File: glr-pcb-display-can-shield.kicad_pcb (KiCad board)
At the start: 2 copper layers, 46 x 90 mm, 11 parts, among them CN12 Conn_02x08_Odd_Even, CN6 Conn_01x08, CN8 Conn_01x06, IC1 L9615D013TR, IC2 LF80CDT-TR, J1 Screw_Terminal_01x04, J2 Screw_Terminal_01x08

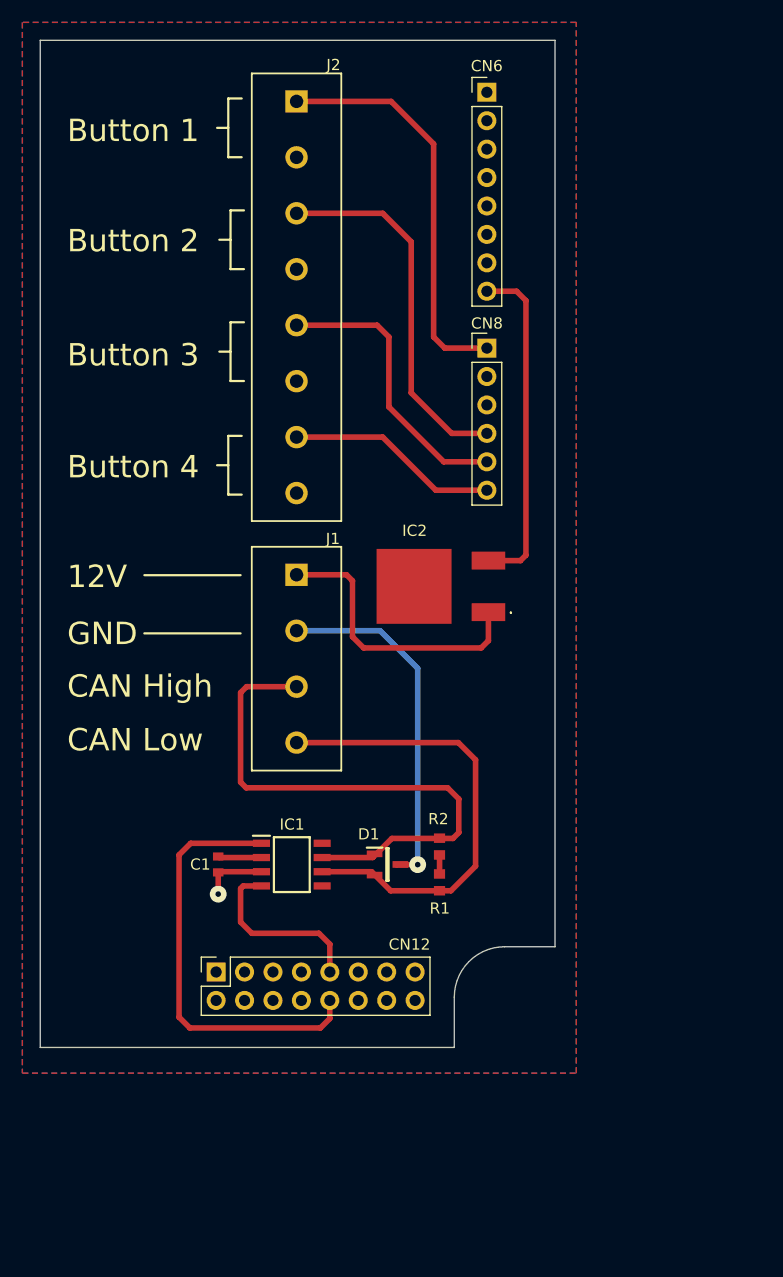
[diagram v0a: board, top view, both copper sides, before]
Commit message: update can shield for new car
* provide more inputs for buttons and rotary encoders (not sure about that, big connector needed now)
* apply new can setup
* add new voltage transformer
* add full arduino headers
* m12a 4pin for power and can
* make board full size
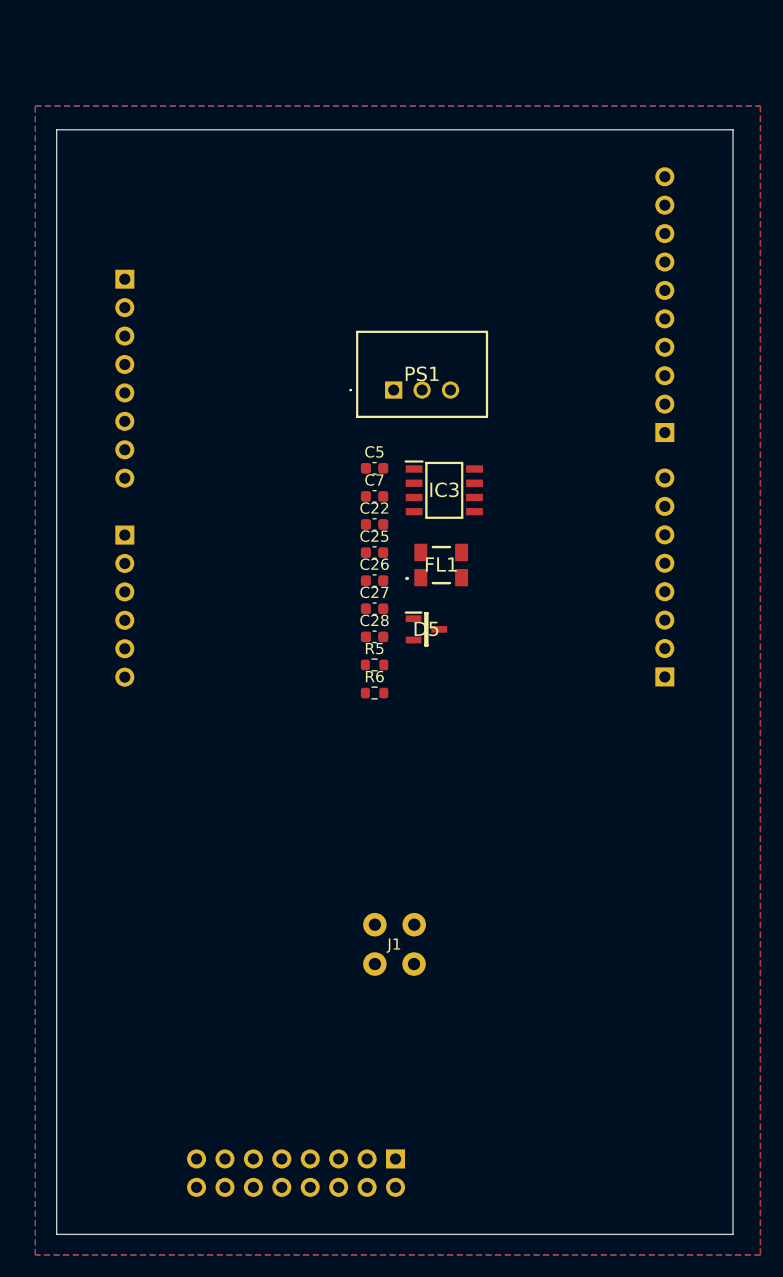
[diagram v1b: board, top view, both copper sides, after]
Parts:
- removed C1: 0.1μF 50V, SamacSys_Parts:CAPC1608X90N
- removed D1: ESDCAN01-2BLY, SamacSys_Parts:SOT95P255X125-3N
- removed IC1: L9615D013TR, SamacSys_Parts:SOIC127P600X175-8N
- removed IC2: LF80CDT-TR, SamacSys_Parts:LF80CDTTR
- removed J2: Screw_Terminal_01x08, GLR_KiCad_Library:WECO-950-FB-08
- removed R1, R2: 68.0 Ω, SamacSys_Parts:RESC1608X50N
- added C22: 100n, Capacitor_SMD:C_0603_1608Metric, F.Cu at (147.5, 88.5)
- added C25: 100p, Capacitor_SMD:C_0603_1608Metric, F.Cu at (147.5, 91.0)
- added C26: 100p, Capacitor_SMD:C_0603_1608Metric, F.Cu at (147.5, 93.5)
- added C27: 100p, Capacitor_SMD:C_0603_1608Metric, F.Cu at (147.5, 96.0)
- added C28: 100p, Capacitor_SMD:C_0603_1608Metric, F.Cu at (147.5, 98.5)
- added C5: 100n, Capacitor_SMD:C_0603_1608Metric, F.Cu at (147.5, 83.5)
- added C7: 100n, Capacitor_SMD:C_0603_1608Metric, F.Cu at (147.5, 86.0)
- added CN5: Conn_01x10, Connector_PinHeader_2.54mm:PinHeader_1x10_P2.54mm_Vertical, B.Cu at (173.4, 80.3)
- added CN7: Conn_01x08, Connector_PinHeader_2.54mm:PinHeader_1x08_P2.54mm_Vertical, B.Cu at (173.4, 102.1)
- added D5: ESDCAN01-2BLY, SamacSys_Parts:SOT95P255X125-3N, F.Cu at (152.1, 97.8)
- added FL1: Choke, SamacSys_Parts:744235510, F.Cu at (153.4, 92.1)
- added IC3: ATA6561-GAQW-N, SamacSys_Parts:SOIC127P600X175-8N, F.Cu at (153.7, 85.4)
- added PS1: RBT05W24S6V5, SamacSys_Parts:RBT05W24S6V5, F.Cu at (149.2, 76.5)
- added R5: 60, Resistor_SMD:R_0603_1608Metric, F.Cu at (147.5, 101.0)
- added R6: 60, Resistor_SMD:R_0603_1608Metric, F.Cu at (147.5, 103.5)
- CN12, CN6, CN8: moved to B.Cu
- J1: value Screw_Terminal_01x04 -> Conn_02x02_Counter_Clockwise_Shielded; footprint GLR_KiCad_Library:WECO-950-FB-04 -> GLR_KiCad_Library:M12A-04P
- moved CN6 36.4 mm to (125.2, 66.6), turned to 180 degrees
- moved CN8 36.4 mm to (125.2, 89.4), turned to 180 degrees
- moved CN12 23.2 mm to (149.3, 145.2)
- moved J1 17.6 mm to (149.2, 126.0), turned to 0 degrees
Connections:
- CN12 pad 10: /Tx -> can_TX
- CN12 pad 3: unconnected-(CN12-Pin_3-Pad3) -> pot1
- CN12 pad 5: unconnected-(CN12-Pin_5-Pad5) -> pot2
- CN12 pad 6: unconnected-(CN12-Pin_6-Pad6) -> pot3
- CN12 pad 9: /Rx -> can_RX
- CN8 pad 1: /button1 -> button1
- CN8 pad 4: /button2 -> button2
- CN8 pad 5: /button3 -> button3
- CN8 pad 6: /button4 -> button4
- J1 pad 1: /+12V -> GND
- J1 pad 2: GND -> can_H
- J1 pad 3: /CAN H -> can_L
- J1 pad 4: /CAN L -> +24V
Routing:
- net /CAN H: track 49.5 -> 0.00 mm
- net /CAN L: track 41.5 -> 0.00 mm
- net /Tx: track 38.1 -> 0.00 mm
- net /button1: track 36.4 -> 0.00 mm
- net GND: track 35.6 -> 0.00 mm, vias 1 -> 0
- net /button2: track 33.1 -> 0.00 mm
- net +8V: track 30.1 -> 0.00 mm
- net /button3: track 25.9 -> 0.00 mm
- net /+12V: track 25.6 -> 0.00 mm
- net /button4: track 19.1 -> 0.00 mm
- net /Rx: track 16.2 -> 0.00 mm
- net +5V: track 5.83 -> 0.00 mm, vias 1 -> 0
- net Net-(R1-Pad2): track 1.61 -> 0.00 mm
- added copper zone on F.Cu, net +5V
- added copper zone on B.Cu, net GND
- removed copper zone on B.Cu, net +5V
- removed copper zone on F.Cu, net GND
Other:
- board size 46 x 90 mm -> 60.4 x 98.7 mm
- board text removed: "12V"
- board text removed: "Button 1"
- board text removed: "Button 2"
- board text removed: "Button 3"
- board text removed: "Button 4"
- board text removed: "CAN High"
- board text removed: "CAN Low"
- board text removed: "GND"

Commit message: use absolute rotary encoders
* use more pins add dsub connector
* add documents
* routing should be done
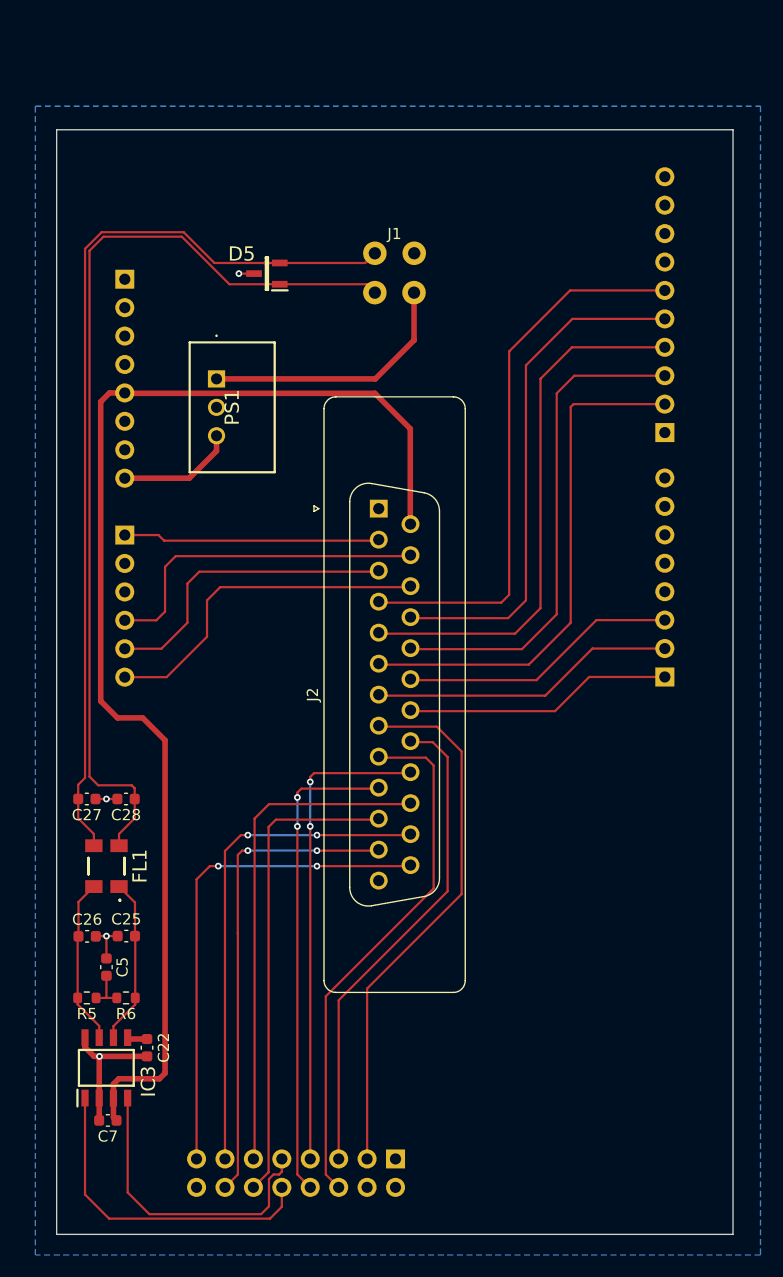
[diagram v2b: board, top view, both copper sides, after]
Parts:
- added J2: DB25_Socket, Connector_Dsub:DSUB-25_Socket_Vertical_P2.77x2.84mm, F.Cu at (147.8, 87.1)
- moved C7 60.6 mm to (123.6, 141.7), turned to 180 degrees
- moved J1 60.0 mm to (149.2, 66.0)
- moved IC3 59.8 mm to (123.5, 137.0), turned to 90 degrees
- moved C22 51.0 mm to (127.1, 135.2), turned to 90 degrees
- moved C5 50.6 mm to (123.5, 128.0), turned to -90 degrees
- moved C26 40.9 mm to (121.8, 125.3), turned to 180 degrees
- moved C25 40.8 mm to (125.3, 125.2), turned to 180 degrees
- moved FL1 40.2 mm to (123.5, 119.0), turned to 90 degrees
- moved R5 39.3 mm to (121.8, 130.8), turned to 180 degrees
- moved R6 35.2 mm to (125.3, 130.8), turned to 180 degrees
- moved D5 34.8 mm to (137.8, 66.0), turned to 180 degrees
- moved C27 30.8 mm to (121.8, 113.0), turned to 180 degrees
- moved C28 26.5 mm to (125.3, 113.0), turned to 180 degrees
- moved PS1 15.9 mm to (133.3, 75.5), turned to -90 degrees
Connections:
- C25 pad 1: can_L -> Net-(IC3-CANL)
- C26 pad 2: can_H -> Net-(IC3-CANH)
- CN12 pad 11: unconnected-(CN12-Pin_11-Pad11) -> absEnc2_P3
- CN12 pad 12: unconnected-(CN12-Pin_12-Pad12) -> absEnc3_P1
- CN12 pad 13: unconnected-(CN12-Pin_13-Pad13) -> absEnc3_P2
- CN12 pad 14: unconnected-(CN12-Pin_14-Pad14) -> absEnc3_P3
- CN12 pad 15: unconnected-(CN12-Pin_15-Pad15) -> absEnc3_P4
- CN12 pad 3: pot1 -> absEnc1_P1
- CN12 pad 5: pot2 -> absEnc1_P2
- CN12 pad 6: pot3 -> absEnc1_P3
- CN12 pad 7: unconnected-(CN12-Pin_7-Pad7) -> absEnc2_P1
- CN12 pad 8: unconnected-(CN12-Pin_8-Pad8) -> absEnc2_P2
- CN5 pad 2: rotenc1_SW -> incEnc1_SW
- CN5 pad 3: rotenc1_DT -> incEnc1_DT
- CN5 pad 4: rotenc1_CLK -> incEnc1_CLK
- CN7 pad 1: rotenc2_SW -> incEnc2_SW
- CN7 pad 2: rotenc2_DT -> incEnc2_DT
- CN7 pad 3: rotenc2_CLK -> incEnc2_CLK
- FL1 pad 1: can_L -> Net-(IC3-CANL)
- FL1 pad 4: can_H -> Net-(IC3-CANH)
- IC3 pad 6: can_L -> Net-(IC3-CANL)
- IC3 pad 7: can_H -> Net-(IC3-CANH)
- R5 pad 2: can_H -> Net-(IC3-CANH)
- R6 pad 1: can_L -> Net-(IC3-CANL)
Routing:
- net +5V: track 0.00 -> 110.0 mm
- net can_L: track 0.00 -> 85.3 mm
- net can_H: track 0.00 -> 82.2 mm
- net button5: track 0.00 -> 49.9 mm
- net absEnc1_P1: track 0.00 -> 48.3 mm
- net incEnc1_CLK: track 0.00 -> 48.2 mm
- net absEnc1_P3: track 0.00 -> 47.4 mm
- net incEnc1_SW: track 0.00 -> 46.5 mm
- net button6: track 0.00 -> 46.1 mm
- net absEnc2_P3: track 0.00 -> 44.9 mm
- net absEnc3_P2: track 0.00 -> 44.7 mm, vias 0 -> 2
- net absEnc3_P4: track 0.00 -> 44.6 mm, vias 0 -> 2
- net incEnc1_DT: track 0.00 -> 44.4 mm
- net absEnc1_P2: track 0.00 -> 43.8 mm
- net absEnc2_P1: track 0.00 -> 43.2 mm, vias 0 -> 2
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- removed copper zone on F.Cu, net +5V

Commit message: setup as aisler project
* update glr library
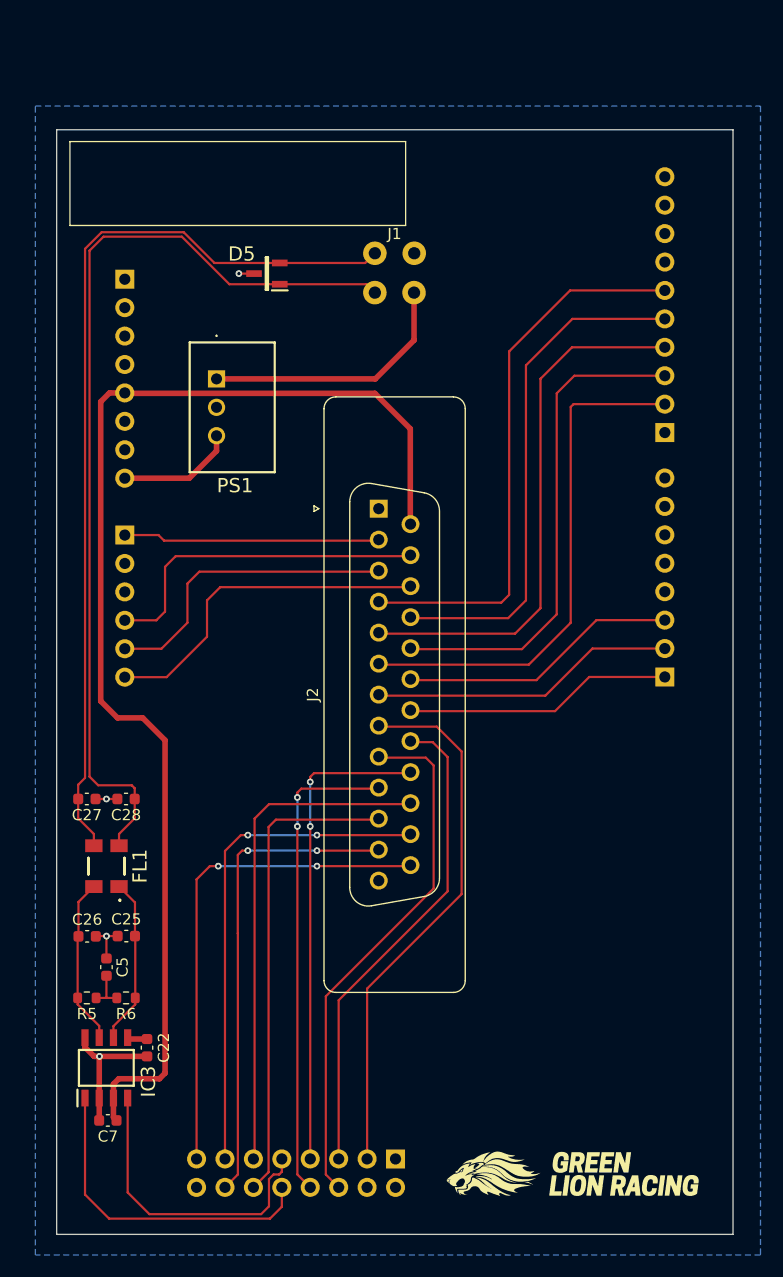
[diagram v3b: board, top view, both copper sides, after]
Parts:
- added G***: LOGO, GLR_KiCad_Library:glr-logo, F.Cu at (165.2, 146.5)

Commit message: replace voltage regulator with buck converter
*
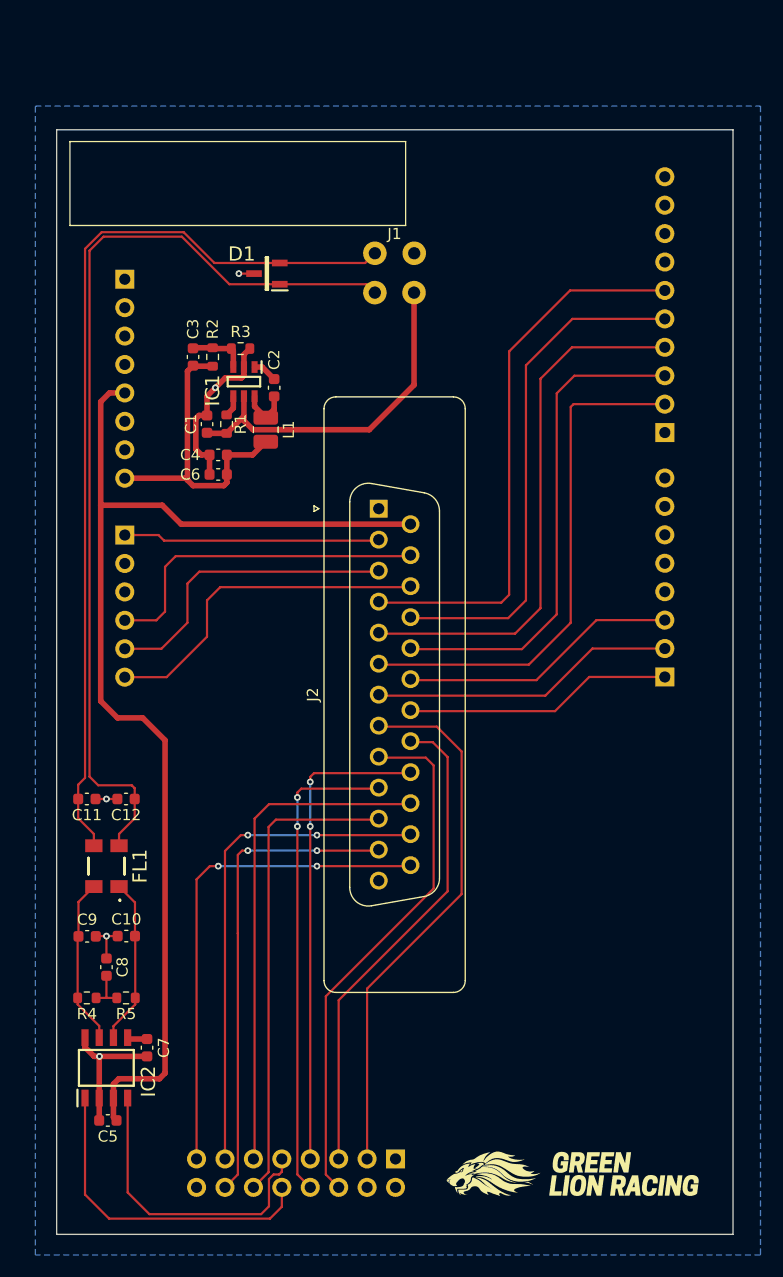
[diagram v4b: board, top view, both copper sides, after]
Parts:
- removed PS1: RBT05W24S6V5, SamacSys_Parts:RBT05W24S6V5
- added C1: 2u2, Capacitor_SMD:C_0603_1608Metric, F.Cu at (132.5, 79.5)
- added C2: 100n, Capacitor_SMD:C_0603_1608Metric, F.Cu at (138.5, 76.2)
- added C3: 100n, Capacitor_SMD:C_0603_1608Metric, F.Cu at (131.2, 73.5)
- added C4: 1u, Capacitor_SMD:C_0603_1608Metric, F.Cu at (133.5, 82.2)
- added C6: 100n, Capacitor_SMD:C_0603_1608Metric, F.Cu at (133.5, 84.0)
- added IC1: AP64060WU-7, SamacSys_Parts:SOT95P280X100-6N, F.Cu at (135.8, 75.7)
- added L1: 18u, Inductor_SMD:L_1008_2520Metric, F.Cu at (137.8, 80.0)
- added R1: 10k, Resistor_SMD:R_0603_1608Metric, F.Cu at (134.2, 79.5)
- added R2: 200k, Resistor_SMD:R_0603_1608Metric, F.Cu at (133.0, 73.5)
- added R3: 22.1k, Resistor_SMD:R_0603_1608Metric, F.Cu at (135.5, 72.8)
- renumbered C25 to C10, C27 to C11, C28 to C12, C7 to C5, C22 to C7, C5 to C8, C26 to C9, D5 to D1, IC3 to IC2, R5 to R4, R6 to R5
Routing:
- net +8V: track 10.6 -> 28.2 mm
- net GND: track 19.7 -> 35.2 mm, vias 4 -> 5
- net +24V: track 23.3 -> 31.6 mm
- net +5V: track 110.0 -> 102.9 mm
- net Net-(IC1-FB): track 0.00 -> 5.20 mm
- net Net-(IC1-SW): track 0.00 -> 4.55 mm
- net Net-(IC1-BST): track 0.00 -> 2.20 mm
- net Net-(IC1-EN): track 0.00 -> 1.92 mm
